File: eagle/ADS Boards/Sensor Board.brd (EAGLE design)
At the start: 69.8 x 69.8 mm, 19 parts

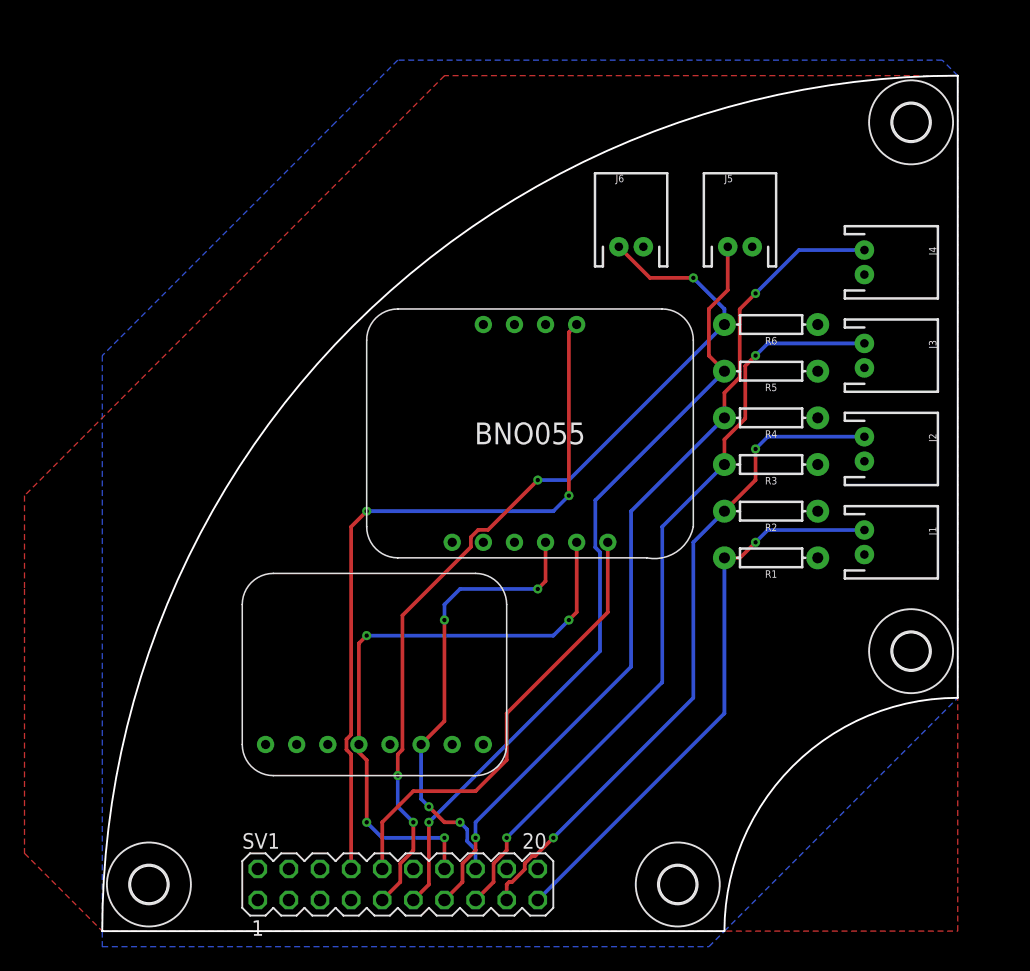
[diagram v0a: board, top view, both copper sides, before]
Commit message: Modify to surface mount components
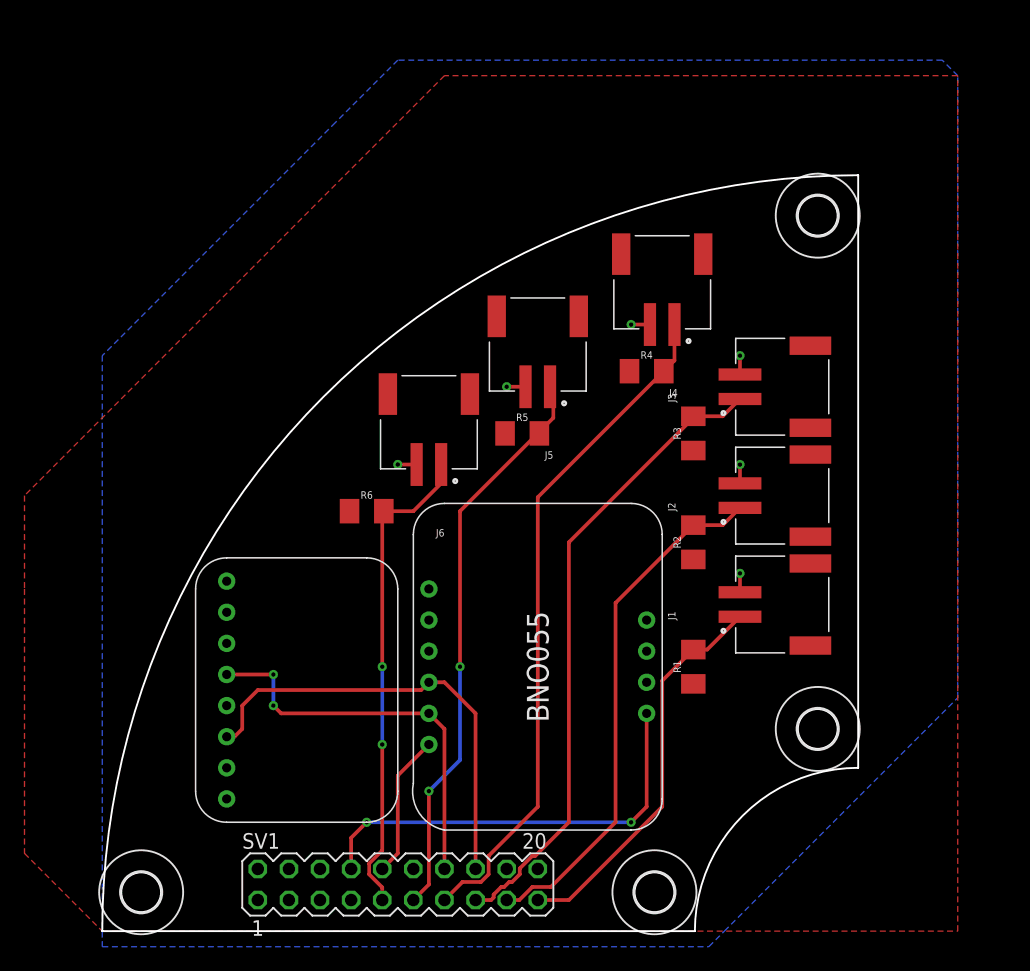
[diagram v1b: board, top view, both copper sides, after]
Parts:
- H1, H2, H3, H4: value MOUNT-HOLE3.0 -> MOUNT-HOLE3.2; device holes:3,0 -> holes:3,2
- J1, J2, J3, J4, J5, J6: value (none) -> S2B-PH-SM4-TB(LF)(SN); device SparkFun-Connectors:JST-2-PTH -> S2B-PH-SM4-TB_LF__SN_:JST_S2B-PH-SM4-TB(LF)(SN)
- R1, R2, R3, R4, R5, R6: device SparkFun-Resistors:AXIAL-0.3 -> resistor:M1206
- moved R6 36.4 mm to (21.6, 34.3), turned to 0 degrees
- moved J6 24.3 mm to (26.7, 38.1), turned to 180 degrees
- moved R5 20.9 mm to (34.3, 40.6), turned to 0 degrees
- moved J5 20.1 mm to (35.6, 44.5), turned to 180 degrees
- moved U$1 18.2 mm to (7.62, 30.5), turned to 270 degrees
- moved J4 17.3 mm to (45.7, 49.5), turned to 180 degrees
- moved J1 11.4 mm to (52.1, 26.7), turned to 90 degrees
- moved R1 10.9 mm to (48.3, 21.6), turned to 90 degrees
- moved R4 10.9 mm to (44.5, 45.7), turned to 0 degrees
- moved J2 10.9 mm to (52.1, 35.6), turned to 90 degrees
- moved H4 10.8 mm to (58.4, 58.4)
- moved J3 10.5 mm to (52.1, 44.5), turned to 90 degrees
- moved H3 9.92 mm to (58.4, 16.5)
- moved R2 6.84 mm to (48.3, 31.8), turned to 90 degrees
- moved R3 6.84 mm to (48.3, 40.6), turned to 90 degrees
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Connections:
- net 3.3V: now also R1.1, R2.1, R3.1, R4.1, R5.1, R6.1; no longer R1.P$1, R2.P$1, R3.P$1, R4.P$1, R5.P$1, R6.P$1
- net B1: now also R1.2; no longer R1.P$2
- net B2: now also R2.2; no longer R2.P$2
- net B3: now also R3.2; no longer R3.P$2
- net B4: now also R4.2; no longer R4.P$2
- net B5: now also R5.2; no longer R5.P$2
- net B6: now also R6.2; no longer R6.P$2
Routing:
- net B6: track 73.6 -> 40.1 mm, vias 4 -> 2
- net ADR: track 61.3 -> 35.3 mm
- net RST: track 37.3 -> 11.7 mm
- net B5: track 65.3 -> 46.8 mm, vias 1 -> 2
- net SCL: track 48.8 -> 32.5 mm, vias 4 -> 2
- net B4: track 70.4 -> 55.7 mm, vias 2 -> 0
- net B1: track 46.6 -> 32.1 mm, vias 1 -> 0
- net B2: track 54.8 -> 42.8 mm, vias 2 -> 0
- net B3: track 63.2 -> 52.4 mm, vias 2 -> 0
- net GND: track 0.00 -> 9.24 mm, vias 0 -> 6
- net SDA: track 37.2 -> 37.0 mm, vias 4 -> 0
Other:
- board size 69.8 x 69.8 mm -> 61.7 x 61.7 mm

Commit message: Finalized Boards, Gerbers, and DXF files.
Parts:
- removed SV1: (no value), con-lstb:MA10-2
- added J7: 62674-121121ALF, NUSTARS ADS Library:CON12_1X12_DUT_58XF
- R1, R2, R3, R4, R5, R6: device resistor:M1206 -> resistor:R0805
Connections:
- net 3.3V: now also J7.1; no longer SV1.20
- net ADR: now also J7.11; no longer SV1.8
- net B1: now also J7.4; no longer SV1.19
- net B2: now also J7.5; no longer SV1.17
- net B3: now also J7.6; no longer SV1.15
- net B4: now also J7.7; no longer SV1.13
- net B5: now also J7.8; no longer SV1.11
- net B6: now also J7.9; no longer SV1.9
- net GND: now also J7.12; no longer SV1.1
- net RST: now also J7.10; no longer SV1.10
- net SCL: now also J7.3; no longer SV1.14
- net SDA: now also J7.2; no longer SV1.16
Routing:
- net B1: track 32.1 -> 41.9 mm
- net B3: track 52.4 -> 59.5 mm, vias 0 -> 2
- net B2: track 42.8 -> 49.5 mm, vias 0 -> 2
- net ADR: track 35.3 -> 32.2 mm
- net B6: track 40.1 -> 37.2 mm
- net B4: track 55.7 -> 58.3 mm, vias 0 -> 2
- net RST: track 11.7 -> 13.6 mm
- net GND: track 9.24 -> 10.9 mm, vias 6 -> 7
- net SDA: track 37.0 -> 38.2 mm
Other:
- board text added: "10k"
- board text added: "ACTIVE DRAG SYSTEM"
- board text added: "HW Rev. 1"
- board text added: "NUSTARS"
- board text added: "Sensor Board"

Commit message: fixed rocket boards
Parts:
- removed J5, J6: S2B-PH-SM4-TB(LF)(SN), S2B-PH-SM4-TB_LF__SN_:JST_S2B-PH-SM4-TB(LF)(SN)
- removed R3, R4, R5, R6: 10k, resistor:R0805
- J3: value S2B-PH-SM4-TB(LF)(SN) -> (none); device S2B-PH-SM4-TB_LF__SN_:JST_S2B-PH-SM4-TB(LF)(SN) -> SparkFun-Connectors:1X08
- J4: value S2B-PH-SM4-TB(LF)(SN) -> (none); device S2B-PH-SM4-TB_LF__SN_:JST_S2B-PH-SM4-TB(LF)(SN) -> SparkFun-Connectors:1X06
- moved H1 67.3 mm to (3.24, 70.5), turned to 270 degrees
- moved H4 55.8 mm to (69.9, 3.85), turned to 270 degrees
- moved J3 48.9 mm to (3.24, 45.8)
- moved J4 46.8 mm to (52.1, 3.21), turned to 0 degrees
- moved H3 44.3 mm to (15.9, 3.85)
- moved H2 43.9 mm to (3.24, 16.5), turned to 270 degrees
- moved J7 36.5 mm to (7.05, 30.5), turned to 90 degrees
- moved J2 31.5 mm to (34.4, 9.56), turned to 0 degrees
- moved R2 24.2 mm to (32.4, 13.4), turned to 0 degrees
- moved U$1 19.1 mm to (8.95, 49.6), turned to 0 degrees
- moved J1 18.7 mm to (44.5, 9.56), turned to 0 degrees
- moved U$2 13.8 mm to (36.9, 42.6)
- moved R1 9.97 mm to (42.6, 13.4), turned to 0 degrees
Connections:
- removed net B3: J3.1, J7.6, R3.2
- removed net B4: J4.1, J7.7, R4.2
- removed net B5: J5.1, J7.8, R5.2
- removed net B6: J6.1, J7.9, R6.2
- new net S0: J3.4, J4.2
- new net S1: J3.5, J4.3
- new net S2: J3.6, J4.4
- new net S3: J3.7, J4.5
- net 3.3V: now also J3.1, J4.1; no longer R3.1, R4.1, R5.1, R6.1
- net GND: now also J3.8, J4.6; no longer J3.2, J4.2, J5.2, J6.2
- net SCL: now also J3.3
- net SDA: now also J3.2
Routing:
- net S3: track 0.00 -> 98.6 mm, vias 0 -> 1
- net S2: track 0.00 -> 94.3 mm, vias 0 -> 1
- net S1: track 0.00 -> 90.7 mm, vias 0 -> 1
- net S0: track 0.00 -> 89.2 mm, vias 0 -> 1
- net ADR: track 32.2 -> 94.9 mm, vias 2 -> 3
- net RST: track 13.6 -> 73.7 mm, vias 0 -> 3
- net B3: track 59.5 -> 0.00 mm, vias 2 -> 0
- net B4: track 58.3 -> 0.00 mm, vias 2 -> 0
- net SCL: track 32.3 -> 86.4 mm
- net B5: track 47.2 -> 0.00 mm, vias 2 -> 0
- net SDA: track 38.2 -> 80.6 mm, vias 0 -> 3
- net B6: track 37.2 -> 0.00 mm, vias 2 -> 0
- net B1: track 41.9 -> 78.5 mm, vias 0 -> 4
- net B2: track 49.5 -> 75.3 mm, vias 2 -> 4
- net GND: track 10.9 -> 4.92 mm, vias 7 -> 3
- added copper zone on layer 1, net D2
- added copper zone on layer 1, net DUMMY
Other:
- board size 61.7 x 61.7 mm -> 73 x 73 mm
- board text added: "3.3V"
- board text added: "B1"
- board text added: "B2"
- board text added: "C:/Users/ichis/Pictures/Cornket.bmp"
- board text added: "C:/Users/ichis/Pictures/NUSTARS Logo PNG.bmp"
- board text added: "GND"
- board text added: "Hardware Ver. 1.1"
- board text added: "S0"
- board text added: "S1"
- board text added: "S2"
- board text added: "S3"
- board text added: "SCA"
- board text added: "SCL"
- board text added: "oh sh*t headers"
- board text removed: "HW Rev. 1"
- board text removed: "NUSTARS"
